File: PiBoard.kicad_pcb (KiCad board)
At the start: 4 copper layers, 95.7 x 102.3 mm, 171 parts, among them IC1 TCAN337DCNR, IC2 TPS2066TDGNRQ1, IC3 TPS2066TDGNRQ1, IC4 AP64501QSP-13, IC5 74LVC1G07QSE-7, IC6 TPS2553QDBVRQ1, IC8 LM76202QPWPRQ1, J1 CarPowerConnector, J10 M8 USB Conn, J11 CarCANConnector, J12 RTC Battery Port, J2 CarCANConnector, J3 2222, J4 USB_OTG, J5 M8 USB Conn, J6 M8 USB Conn, J7 Molex 470531000, J8 M8 USB Conn, J9 HDMI_E, SW1 SW_Push, SW2 SW_Push, SW3 SW_Push, U1 RTC PCF8563T, U10 Fan PWM Controller, U13 CDSOT23-T24CAN, U14 MCP2515-E/STVAO, U2 TLV71311PDBV, U3 FSUSB42MUX, U4 TUSB4041IPAPQ1, U5 TPD4EUSB30, U6 TPD4EUSB30, U7 TPD4EUSB30, Y1 24MHz Crystal, Y4 8 MHz, Y6 ECS-.327-6

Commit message: moved some stuff around
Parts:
- C14, C17, C18, C22, C23, C24, C25, C26, C27, C3, C32, C33, C36, C37, C43, C51, C54, C56, C59, C60, D10, D6, F1, F2, F3, F4, FB1, FB2, FB3, FB4, FB5, FB6, IC6, R11, R14, R16, R17, R18, R19, R2, R21, R22, R23, R27, R28, R30, R31, R32, R34, R40, R43, U13, Y6: moved to B.Cu
- C6, R55, R56: moved to F.Cu
- R44: value 5k -> 10k
- R46: value 6.8k -> 12k
- moved R41 82.9 mm to (234.5, 153.2)
- moved R43 79.6 mm to (232.7, 150.5), turned to 180 degrees
- moved R8 74.6 mm to (231.8, 154.4), turned to 0 degrees
- moved R40 74.6 mm to (229.3, 150.5), turned to 0 degrees
- moved D11 73.9 mm to (235.5, 147.8), turned to -90 degrees
- moved R46 73.9 mm to (235.5, 149.8), turned to 90 degrees
- moved IC8 73.5 mm to (230.6, 149.5), turned to 90 degrees
- moved C3 71.9 mm to (227.7, 106.6)
- moved C54 70.9 mm to (232.7, 148.5), turned to 180 degrees
- moved R27 70.2 mm to (227.6, 110.0)
- moved R42 67.5 mm to (229.2, 144.5), turned to 0 degrees
- moved R7 66.6 mm to (226.7, 151.8), turned to -90 degrees
- moved IC6 65.9 mm to (224.8, 107.4)
- moved C43 65.6 mm to (224.4, 104.2), turned to 0 degrees
- moved R28 65.0 mm to (224.7, 110.4), turned to 180 degrees
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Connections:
- net +12V renamed +24V
- net +12V_EXT renamed +24V_EXT
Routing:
- net /Board_En: track 91.5 -> 0.00 mm
- net /CM4 GPIO/GPIO3: track 76.3 -> 0.00 mm, vias 1 -> 0
- net Net-(Module1A-PI_nLED_Activity): track 69.3 -> 0.00 mm, vias 1 -> 0
- net /CM4 GPIO/CAN_SPI_CLK: track 60.1 -> 0.00 mm, vias 1 -> 0
- net /CM4 GPIO/nPWR_LED: track 59.4 -> 0.00 mm
- net /CM4 GPIO/CAN_SPI_MOSI: track 53.3 -> 0.00 mm, vias 3 -> 0
- net /CM4 GPIO/CAN_SPI_CS: track 52.8 -> 0.00 mm, vias 2 -> 0
- net /CM4 GPIO/CAN_SPI_MISO: track 51.5 -> 0.00 mm, vias 3 -> 0
- net /HDMI and High Speed/HDMI0_CK_N: track 50.2 -> 0.00 mm
- net /HDMI and High Speed/HDMI0_CK_P: track 50.1 -> 0.00 mm
- net Net-(IC1-CANH): track 50.0 -> 0.00 mm, vias 1 -> 0
- net /CM4 GPIO/CAN_INTR: track 49.4 -> 0.00 mm
- net /USB2.0 HS Hub/USB_Ports/USB_4P: track 48.2 -> 0.00 mm, vias 1 -> 0
- net /USB2.0 HS Hub/USB_Ports/USB_4N: track 46.7 -> 0.00 mm, vias 1 -> 0
- net /USB2.0 HS Hub/USB_Upstream_N: track 46.6 -> 0.00 mm, vias 2 -> 0
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
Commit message: layout draft
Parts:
- removed C18, C19, C29, C32, C33, C34, C35, C38, C39, C40, C41, C42, C44, C45, C46, C47, C48, C49: 100n, Capacitor_SMD:C_0805_2012Metric
- removed C26, C27: 25p, Capacitor_SMD:C_0805_2012Metric
- removed C28: 1u, Capacitor_SMD:C_0805_2012Metric
- removed C30, C31: 1n, Capacitor_SMD:C_0805_2012Metric
- removed F1, F2, F3, F4: 500mA, Fuse:Fuse_1206_3216Metric
- removed FB3, FB4, FB5, FB6: FerriteBead, Inductor_SMD:L_1206_3216Metric
- removed IC3: TPS2066TDGNRQ1, Controls_Pi:SOP65P490X110-9N
- removed J10, J6, J8: M8 USB Conn, Controls_Pi:321720912
- removed R13, R14, R33, R55, R56: 10k, Resistor_SMD:R_0805_2012Metric
- removed R15, R20: 1M, Resistor_SMD:R_0805_2012Metric
- removed R36, R50, R51, R52, R53, R54: 4.7k, Resistor_SMD:R_0805_2012Metric
- removed U2: TLV71311PDBV, Package_TO_SOT_SMD:SOT-23-5
- removed U4: TUSB4041IPAPQ1, Controls_Pi:PAP64_4P15X4P15_TEX
- removed U5, U6, U7: TPD4EUSB30, Package_SON:USON-10_2.5x1.0mm_P0.5mm
- removed Y1: 24MHz Crystal, Controls_Pi:ABM8AIG25000MHZ122ZT3
- added C57: 100n, Capacitor_SMD:C_0805_2012Metric, B.Cu at (176.2, 94.3)
- added C58: 10uF, Capacitor_SMD:C_0805_2012Metric, F.Cu at (149.3, 56.5)
- added D15: ESD204DQAR, Controls_Pi:ESD204DQAR, F.Cu at (180.7, 92.1)
- added D18: ESD204DQAR, Controls_Pi:ESD204DQAR, F.Cu at (180.7, 79.9)
- added H1: MountingHole, MountingHole:MountingHole_3mm, F.Cu at (106.0, 55.6)
- added H2: MountingHole, MountingHole:MountingHole_3mm, F.Cu at (187.4, 55.5)
- added H3: MountingHole, MountingHole:MountingHole_3mm, F.Cu at (106.0, 139.7)
- added H4: MountingHole, MountingHole:MountingHole_3mm, F.Cu at (187.6, 139.1)
- added IC7: TPS2553QDBVRQ1, Controls_Pi:SOT95P280X145-6N, F.Cu at (176.1, 97.5)
- added J13: RTC Battery Conn, Controls_Pi:CONN02_530470210_MOL, F.Cu at (185.1, 64.3)
- added R37: 5.1k, Resistor_SMD:R_0805_2012Metric, B.Cu at (188.4, 94.2)
- added R38: 5.1k, Resistor_SMD:R_0805_2012Metric, B.Cu at (188.4, 90.8)
- added R62: 100n, Resistor_SMD:R_0805_2012Metric, F.Cu at (173.1, 97.4)
- added R69: 82k, Resistor_SMD:R_0805_2012Metric, B.Cu at (177.1, 101.4)
- C1, C10, C12, C2, C20, C21, R24, R26, R29, R3, R41: moved to B.Cu
- C13: value 100n -> 1n; moved to B.Cu
- C15: value 1n -> 100n
- D3: value SD12_SOD323 -> SD24C_SOD323
- D6, U13: moved to F.Cu
- D9: value 12V PWR LED -> 24V PWR LED
- IC2: value TPS2066TDGNRQ1 -> TPS2553QDBVRQ1; footprint Controls_Pi:SOP65P490X110-9N -> Controls_Pi:SOT95P280X145-6N
- J4: value USB_OTG -> USB_C_Receptacle_USB2.0_16P; footprint Connector_USB:USB_Micro-B_Molex-105017-0001 -> Connector_USB:USB_C_Receptacle_GCT_USB4105-xx-A_16P_TopMnt_Horizontal
- J5: value M8 USB Conn -> USB_C_Receptacle_USB2.0_16P; footprint Controls_Pi:321720912 -> Connector_USB:USB_C_Receptacle_GCT_USB4105-xx-A_16P_TopMnt_Horizontal
- R10: value 1M -> 5.1k; moved to B.Cu
- R11: value 90.9k -> 1M
- R12: value 9.53k -> 1M; moved to B.Cu
- R40: value 1k -> 10k; moved to F.Cu
- R46: value 12k -> 10k
- R5: value 1M -> 100n; moved to F.Cu
- R6: value 1M -> 82k
- R7: value 100k -> 200k
- R8: value 200 -> 2k
- R9: value 2.2k -> 5.1k; moved to B.Cu
- moved C16 169.3 mm to (190.7, 76.7), turned to -90 degrees
- moved C17 162.9 mm to (190.7, 83.8)
- moved J5 158.0 mm to (187.6, 80.2), turned to 90 degrees
- moved FB2 157.8 mm to (181.5, 97.1)
- moved R6 154.3 mm to (176.7, 88.8), turned to 90 degrees
- moved FB1 154.1 mm to (181.2, 84.8)
- moved C15 151.6 mm to (186.5, 97.0), turned to 90 degrees
- moved R5 148.4 mm to (172.8, 84.8), turned to 90 degrees
- moved R9 147.0 mm to (186.6, 82.2)
- moved J7 143.8 mm to (177.2, 57.0), turned to 180 degrees
- moved C13 142.5 mm to (186.6, 88.0), turned to -90 degrees
- moved J4 141.8 mm to (187.5, 92.9), turned to 90 degrees
- moved IC2 140.7 mm to (175.7, 84.8), turned to -90 degrees
- moved C12 140.2 mm to (179.2, 96.5), turned to -90 degrees
- moved U1 138.9 mm to (178.9, 63.3), turned to 180 degrees
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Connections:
- C1 pad 1: +5V -> Net-(IC2-EN)
- C12 pad 1: +5V -> Net-(C12-Pad1)
- C13 pad 1: +5V -> GNDPWR
- C17 pad 1: Net-(C17-Pad1) -> GNDPWR
- C2 pad 1: +1V1 -> +5V
- C4 pad 1: Net-(C38-Pad1) -> Net-(C4-Pad1)
- D10 pad 1: /HDMI and High Speed/HDMI0_CK_N -> /HDMI and High Speed/HDMI0_CK_P
- D10 pad 10: /HDMI and High Speed/HDMI0_CK_PRT_N -> /HDMI and High Speed/HDMI0_CK_PRT_P
- D10 pad 2: /HDMI and High Speed/HDMI0_CK_P -> /HDMI and High Speed/HDMI0_CK_N
- D10 pad 4: /HDMI and High Speed/HDMI0_D1_N -> /HDMI and High Speed/HDMI0_D1_P
- D10 pad 5: /HDMI and High Speed/HDMI0_D1_P -> /HDMI and High Speed/HDMI0_D1_N
- D10 pad 6: /HDMI and High Speed/HDMI0_D1_PRT_P -> /HDMI and High Speed/HDMI0_D1_PRT_N
- D10 pad 7: /HDMI and High Speed/HDMI0_D1_PRT_N -> /HDMI and High Speed/HDMI0_D1_PRT_P
- D10 pad 9: /HDMI and High Speed/HDMI0_CK_PRT_P -> /HDMI and High Speed/HDMI0_CK_PRT_N
- FB1 pad 1: /USB2.0 HS Hub/USB_Ports/VBUS1 -> /USB2.0 high speed/VBUS_Hub
- FB1 pad 2: Net-(C17-Pad1) -> Net-(C4-Pad1)
- FB2 pad 1: /USB2.0 HS Hub/USB_Ports/VBUS2 -> /USB2.0 high speed/VBUS_Debug
- FB2 pad 2: Net-(C18-Pad1) -> Net-(C12-Pad1)
- IC2 pad 1: GND -> +5V
- IC2 pad 2: +5V -> GND
- IC2 pad 3: /USB2.0 HS Hub/USB_Ports/EN1 -> Net-(IC2-EN)
- IC2 pad 4: /USB2.0 HS Hub/USB_Ports/EN2 -> Net-(IC2-EN)
- IC2 pad 5: /USB2.0 HS Hub/USB_Ports/OC2 -> Net-(IC2-ILIM)
- IC2 pad 6: Net-(IC2-OUT2) -> /USB2.0 high speed/VBUS_Hub
- J11 pad 1: Net-(IC1-CANH) -> Net-(IC1-CANL)
- J11 pad 2: Net-(IC1-CANL) -> Net-(IC1-CANH)
- J2 pad 1: Net-(IC1-CANH) -> Net-(IC1-CANL)
- J2 pad 2: Net-(IC1-CANL) -> Net-(IC1-CANH)
- R10 pad 1: Net-(U4A-XI) -> Net-(C4-Pad1)
- R10 pad 2: Net-(U4A-XO) -> Net-(J5-CC2)
- R11 pad 1: +5V -> GND
- R11 pad 2: Net-(U4A-USB_VBUS) -> GNDPWR
- R12 pad 1: Net-(U4A-USB_R1) -> GND
- R12 pad 2: GND -> GNDPWR
- R5 pad 1: GND -> /Board_En
- R5 pad 2: GNDPWR -> Net-(IC2-EN)
- R6 pad 2: GNDPWR -> Net-(IC2-ILIM)
- R9 pad 1: Net-(J4-VBUS) -> Net-(C4-Pad1)
- R9 pad 2: /HDMI and High Speed/USBOTG_ID -> Net-(J5-CC1)
- U3 pad 6: /USB2.0 HS Hub/USB_Upstream_N -> /USB2.0 high speed/USB_Hub_Up_N
- U3 pad 7: /USB2.0 HS Hub/USB_Upstream_P -> /USB2.0 high speed/USB_Hub_Up_P
- U3 pad 8: Net-(J4-D-) -> /USB2.0 high speed/USB_Debug_N
- U3 pad 9: Net-(J4-D+) -> /USB2.0 high speed/USB_Debug_P
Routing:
- net /CM4 GPIO/CAN_SPI_MOSI: track 0.00 -> 65.4 mm, vias 0 -> 1
- net /CM4 GPIO/CAN_SPI_MISO: track 0.00 -> 65.2 mm, vias 0 -> 1
- net /CM4 GPIO/CAN_SPI_CLK: track 0.00 -> 60.5 mm, vias 0 -> 1
- net /CM4 GPIO/GPIO22: track 0.00 -> 58.2 mm, vias 0 -> 1
- net /CM4 GPIO/GPIO17: track 0.00 -> 54.5 mm, vias 0 -> 1
- net /CM4 GPIO/GPIO27: track 0.00 -> 53.5 mm, vias 0 -> 1
- net /CM4 GPIO/GPIO0: track 0.00 -> 53.2 mm, vias 0 -> 1
- net /CM4 GPIO/GPIO6: track 0.00 -> 49.7 mm, vias 0 -> 1
- net /CM4 GPIO/GPIO5: track 0.00 -> 48.4 mm, vias 0 -> 1
- net /CM4 GPIO/GPIO4: track 0.00 -> 47.3 mm, vias 0 -> 1
- net /CM4 GPIO/GPIO3: track 0.00 -> 46.4 mm, vias 0 -> 1
- net /CM4 GPIO/GPIO13: track 0.00 -> 44.9 mm, vias 0 -> 1
- net /CM4 GPIO/GPIO19: track 0.00 -> 40.2 mm, vias 0 -> 1
- net /CM4 GPIO/GPIO2: track 0.00 -> 37.9 mm, vias 0 -> 1
- net /CM4 GPIO/GPIO26: track 0.00 -> 35.5 mm, vias 0 -> 1
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- added copper zone on B.Cu, net GND
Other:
- board size 95.7 x 102.3 mm -> 90.1 x 92.5 mm
- board text added: "Trying to keep this space more open for fancy routing ig"

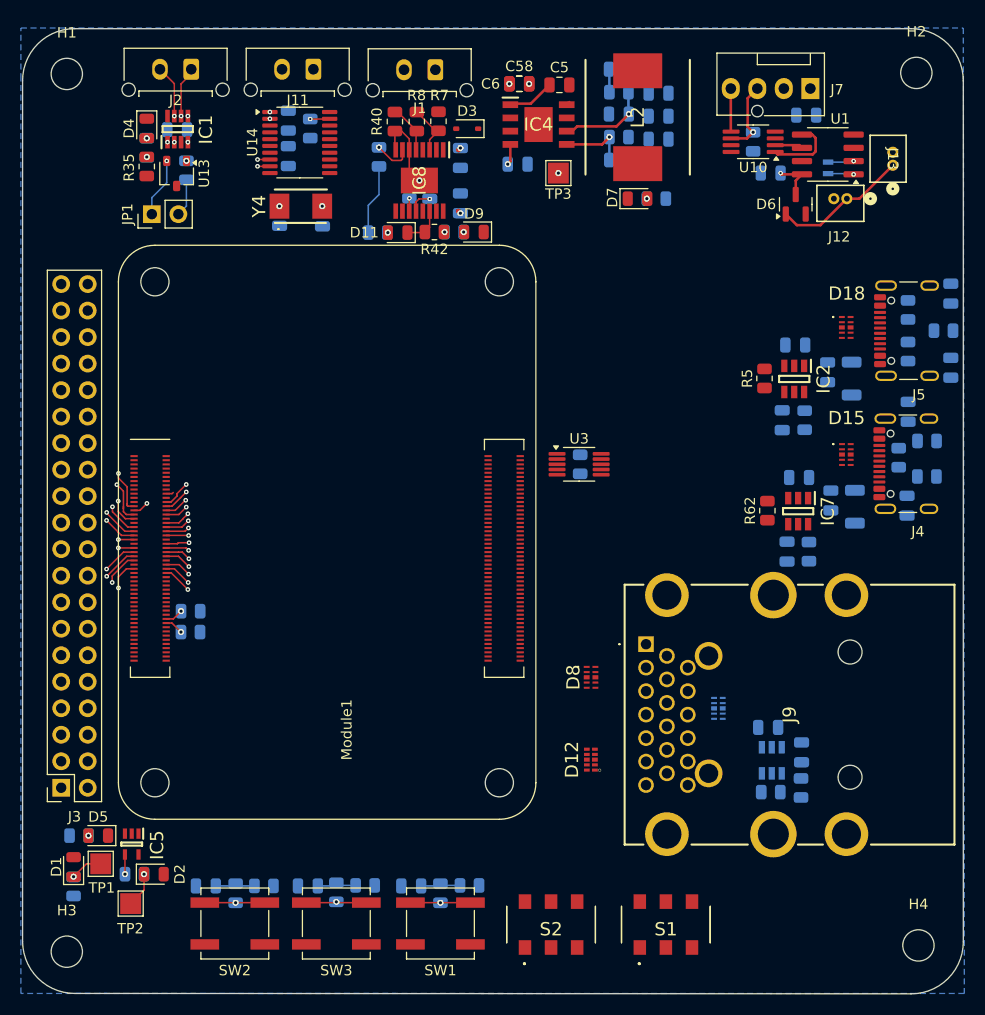
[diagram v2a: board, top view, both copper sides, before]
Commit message: moved everything to front & 0603'd stuff
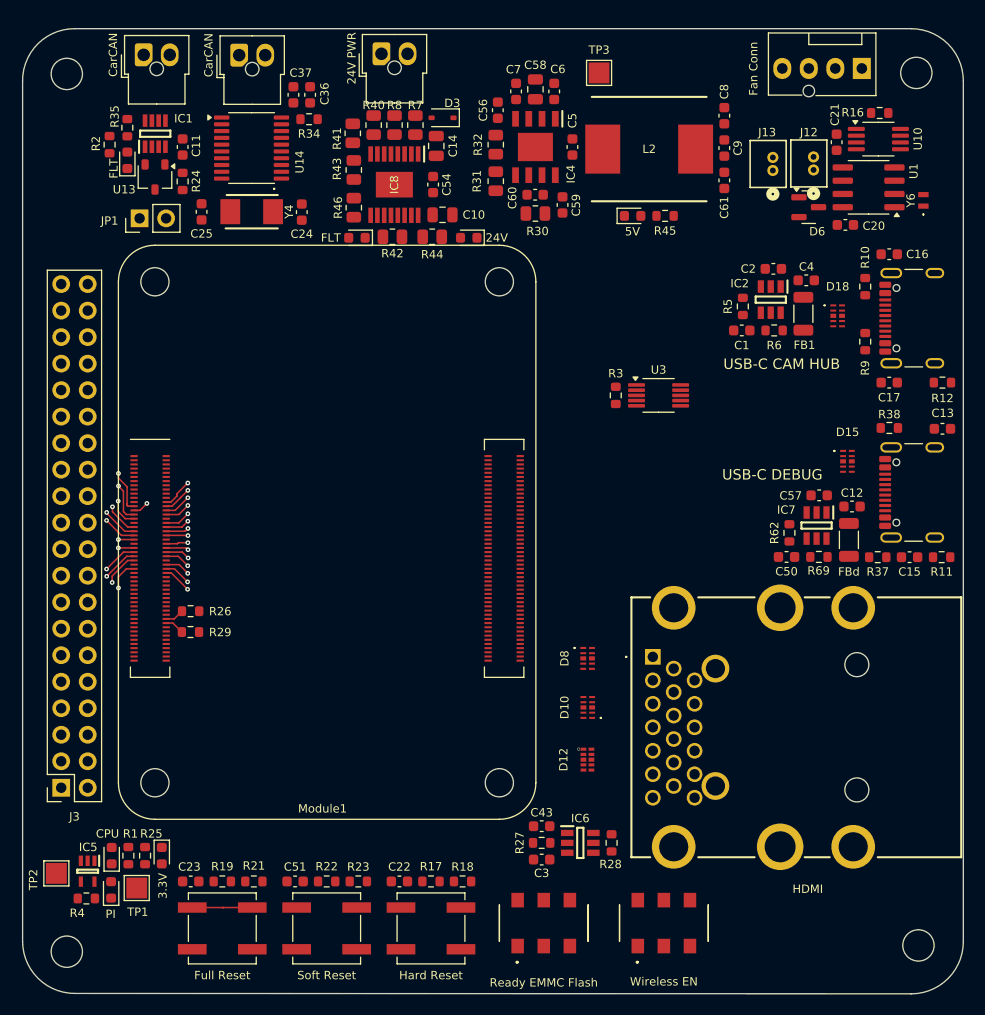
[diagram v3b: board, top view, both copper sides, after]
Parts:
- removed J11, J2: CarCANConnector, Connector_Molex:Molex_Micro-Fit_3.0_43650-0215_1x02_P3.00mm_Vertical
- added CarCAN: CarCANConnector, UTSVT_Connectors:Molex_Nano-Fit_105309-xx02_1x02_P2.50mm_Vertical, F.Cu at (113.4, 53.8)
- added CarCAN: CarCANConnector, UTSVT_Connectors:Molex_Nano-Fit_105309-xx02_1x02_P2.50mm_Vertical, F.Cu at (122.5, 53.8)
- 24V: renamed from D9; footprint LED_SMD:LED_0805_2012Metric -> LED_SMD:LED_0603_1608Metric
- 24V PWR: renamed from J1; footprint Connector_Molex:Molex_Micro-Fit_3.0_43650-0215_1x02_P3.00mm_Vertical -> UTSVT_Connectors:Molex_Nano-Fit_105309-xx02_1x02_P2.50mm_Vertical
- 3.3V: renamed from D5; footprint LED_SMD:LED_0805_2012Metric -> LED_SMD:LED_0603_1608Metric
- 5V: renamed from D7; footprint LED_SMD:LED_0805_2012Metric -> LED_SMD:LED_0603_1608Metric
- C1, C11, C12, C13, C15, C16, C17, C2, C20, C21, C22, C23, C24, C25, C3, C36, C37, C4, C43, C50, C51, C54, C56, C57, C59, C60, C61, C7, C8, C9: footprint Capacitor_SMD:C_0805_2012Metric -> Capacitor_SMD:C_0603_1608Metric; moved to F.Cu
- C10, C14, D10, FB1, IC6, R30, R31, R32, R41, R43, R44, R46, Y6: moved to F.Cu
- C5, C6: footprint Capacitor_SMD:C_0805_2012Metric -> Capacitor_SMD:C_0603_1608Metric
- CPU: renamed from D1; footprint LED_SMD:LED_0805_2012Metric -> LED_SMD:LED_0603_1608Metric
- FBd: renamed from FB2; moved to F.Cu
- FLT: renamed from D11; footprint LED_SMD:LED_0805_2012Metric -> LED_SMD:LED_0603_1608Metric
- FLT: renamed from D4; footprint LED_SMD:LED_0805_2012Metric -> LED_SMD:LED_0603_1608Metric
- Fan Conn: renamed from J7
- Full Reset: renamed from SW2
- Hard Reset: renamed from SW1
- PI: renamed from D2; footprint LED_SMD:LED_0805_2012Metric -> LED_SMD:LED_0603_1608Metric
- R1, R10, R11, R12, R16, R17, R18, R19, R2, R21, R22, R23, R24, R25, R26, R27, R28, R29, R3, R34, R37, R38, R4, R45, R6, R69, R9: footprint Resistor_SMD:R_0805_2012Metric -> Resistor_SMD:R_0603_1608Metric; moved to F.Cu
- R35, R5, R62: footprint Resistor_SMD:R_0805_2012Metric -> Resistor_SMD:R_0603_1608Metric
- Ready EMMC Flash: renamed from S2
- Soft Reset: renamed from SW3
- USB-C CAM HUB: renamed from J5
- USB-C DEBUG: renamed from J4
- Wireless EN: renamed from S1
- moved C3 26.9 mm to (151.5, 130.9), turned to 180 degrees
- moved R27 25.4 mm to (151.5, 129.3), turned to 0 degrees
- moved C43 23.7 mm to (151.5, 127.7), turned to 180 degrees
- moved IC6 20.0 mm to (155.2, 129.3), turned to 0 degrees
- moved R28 16.0 mm to (158.2, 129.3), turned to 90 degrees
- moved R30 14.1 mm to (150.9, 69.0), turned to 0 degrees
- moved C59 14.1 mm to (153.5, 68.2), turned to 90 degrees
- moved D10 12.5 mm to (155.9, 116.3), turned to 180 degrees
- moved R16 12.4 mm to (183.9, 59.3), turned to 0 degrees
- moved U10 12.0 mm to (183.8, 61.8), turned to 0 degrees
- moved R31 12.0 mm to (147.1, 65.9), turned to 90 degrees
- moved R32 11.8 mm to (147.1, 62.4), turned to 90 degrees
- moved C25 11.6 mm to (118.9, 68.8), turned to -90 degrees
- moved J13 11.5 mm to (173.7, 64.8)
- moved C60 11.1 mm to (150.9, 67.2), turned to 0 degrees
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- renumbered J9 to HDMI
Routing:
- net Net-(IC1-CANH): track 28.5 -> 0.00 mm, vias 2 -> 0
- net Net-(IC1-CANL): track 22.2 -> 0.00 mm, vias 2 -> 0
- net /RTC and Fan/RED: track 13.1 -> 0.00 mm
- net /CarCAN/CAN_TX: track 11.0 -> 0.00 mm, vias 2 -> 0
- net /Power Distribution/RTN: track 9.97 -> 0.00 mm, vias 1 -> 0
- net Net-(U14-OSC1): track 9.70 -> 0.00 mm, vias 2 -> 0
- net /CarCAN/CAN_RX: track 8.79 -> 0.00 mm, vias 2 -> 0
- net Net-(IC4-COMP): track 8.74 -> 0.00 mm, vias 1 -> 0
- net Net-(J7-Pin_3): track 7.14 -> 0.00 mm, vias 1 -> 0
- net +24V_EXT: track 7.01 -> 0.00 mm, vias 1 -> 0
- net Net-(U14-OSC2): track 6.98 -> 0.00 mm, vias 2 -> 0
- net /CM4 GPIO/SDA0: track 8.58 -> 1.86 mm, vias 1 -> 0
- net Net-(IC4-FB): track 6.58 -> 0.00 mm, vias 1 -> 0
- net /CarCAN/Fault: track 6.38 -> 0.00 mm, vias 2 -> 0
- net Net-(R22-Pad1): track 5.81 -> 0.00 mm, vias 1 -> 0
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- removed copper zone on B.Cu, net GND
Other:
- board text added: "Left some of these pwr components 0805 (?)"

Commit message: mostly routed, except highspeed
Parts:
- removed J13: RTC Battery Conn, Controls_Pi:CONN02_530470210_MOL
- moved C61 36.9 mm to (133.0, 57.8), turned to 90 degrees
- moved C8 36.3 mm to (133.0, 64.0), turned to -90 degrees
- moved C9 36.0 mm to (133.0, 60.9), turned to -90 degrees
- moved R45 28.8 mm to (138.7, 54.4), turned to 0 degrees
- moved C14 28.7 mm to (170.1, 63.4)
- moved 24V 28.5 mm to (173.0, 72.9)
- moved R44 28.4 mm to (169.3, 72.9)
- moved R42 28.3 mm to (165.4, 72.9)
- moved D3 27.5 mm to (169.5, 59.7)
- moved FLT 27.4 mm to (161.1, 73.1)
- moved C10 27.3 mm to (169.3, 70.2)
- moved C54 27.3 mm to (168.4, 67.0)
- moved R7 27.2 mm to (166.6, 60.9)
- moved 24V PWR 26.9 mm to (163.1, 53.7)
- moved R8 26.9 mm to (164.3, 60.9)
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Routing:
- net GND: track 0.00 -> 187.0 mm, vias 0 -> 67
- net /Board_En: track 0.00 -> 129.2 mm, vias 0 -> 4
- net /CM4 GPIO/SDA0: track 1.86 -> 104.3 mm, vias 0 -> 4
- net /CM4 GPIO/SCL0: track 1.82 -> 99.6 mm, vias 0 -> 4
- net +3.3V: track 0.00 -> 78.4 mm, vias 0 -> 3
- net /CM4 GPIO/EEPROM_nWP: track 0.00 -> 77.9 mm, vias 0 -> 3
- net /CM4 GPIO/BT_Disable: track 0.00 -> 73.6 mm, vias 0 -> 3
- net /CM4 GPIO/WiFi_Disable: track 0.00 -> 71.8 mm, vias 0 -> 3
- net +5V: track 0.00 -> 61.6 mm, vias 0 -> 1
- net /CM4 GPIO/nRPIBOOT: track 0.00 -> 59.2 mm, vias 0 -> 3
- net GNDPWR: track 0.00 -> 52.3 mm
- net /CM4 GPIO/CAN_SPI_CS: track 6.85 -> 55.9 mm, vias 1 -> 4
- net /CM4 GPIO/RUN_PG: track 0.00 -> 48.4 mm, vias 0 -> 4
- net /CM4 GPIO/CAN_SPI_MOSI: track 65.4 -> 111.0 mm, vias 1 -> 2
- net /CM4 GPIO/CAN_SPI_CLK: track 60.6 -> 104.1 mm, vias 1 -> 4
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- added copper zone on F.Cu, net +24V
- added copper zone on F.Cu, net +24V_EXT
- added copper zone on F.Cu, net +3.3V
- added copper zone on F.Cu, net +5V
- added copper zone on B.Cu, net GND
- added copper zone on In1.Cu, net GND

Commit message: added new power, but lowkey need to redo a bunch of shit
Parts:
- removed 24V: 24V PWR LED, LED_SMD:LED_0603_1608Metric
- removed 24V PWR: CarPowerConnector, UTSVT_Connectors:Molex_Nano-Fit_105309-xx02_1x02_P2.50mm_Vertical
- removed C10, C14: 10u, Capacitor_SMD:C_0805_2012Metric
- removed C54: 100n, Capacitor_SMD:C_0603_1608Metric
- removed D3: SD24C_SOD323, Diode_SMD:D_SOD-323
- removed FLT: PWR FAULT, LED_SMD:LED_0603_1608Metric
- removed IC8: LM76202QPWPRQ1, Controls_Pi:SOP65P640X120-17N
- removed R40, R41, R46: 10k, Resistor_SMD:R_0805_2012Metric
- removed R42: 100k, Resistor_SMD:R_0805_2012Metric
- removed R43: 6.65k, Resistor_SMD:R_0805_2012Metric
- removed R7: 200k, Resistor_SMD:R_0805_2012Metric
- removed R8: 2k, Resistor_SMD:R_0805_2012Metric
- added C18: 1u, Capacitor_SMD:C_0603_1608Metric, F.Cu at (168.3, 58.2)
- added C19: 220n, Capacitor_SMD:C_0603_1608Metric, F.Cu at (168.3, 59.8)
- added C26: 22n, Capacitor_SMD:C_0603_1608Metric, F.Cu at (156.2, 63.8)
- added C27: 220u, Capacitor_SMD:C_0603_1608Metric, F.Cu at (156.2, 66.8)
- added D9: 24V PWR LED, LED_SMD:LED_0603_1608Metric, F.Cu at (164.8, 64.8)
- added IC3: LM74502HDDFR, UTSVT_Power_SP:SOT65P280X110-8N, F.Cu at (165.1, 58.0)
- added J1: CarLVPowerConnector, UTSVT_Connectors:Molex_Nano-Fit_105309-xx02_1x02_P2.50mm_Vertical, F.Cu at (157.9, 53.7)
- added Q1: PSMN8R5-40MSDX, UTSVT_Power_SP:PSMN8R5-40MSDX, F.Cu at (159.7, 65.4)
- added R100: 10k, Resistor_SMD:R_0603_1608Metric, F.Cu at (168.3, 56.6)
- added R13: 8k, Resistor_SMD:R_0603_1608Metric, F.Cu at (165.2, 55.0)
- added R14: 200k, Resistor_SMD:R_0603_1608Metric, F.Cu at (168.3, 55.1)
- added Z1: SMAF4751A-TP, UTSVT_Passives:SODFL5026X125N, F.Cu at (166.5, 62.2)
- added Z2: SMAF4751A-TP, UTSVT_Passives:SODFL5026X125N, F.Cu at (159.3, 60.5)
- J4: renamed from USB-C DEBUG
- J5: renamed from USB-C CAM HUB
- J7: renamed from Fan Conn
- S1: renamed from Wireless EN
- S2: renamed from Ready EMMC Flash
- SW1: renamed from Hard Reset
- SW2: renamed from Full Reset
- SW3: renamed from Soft Reset
- moved R44 9.30 mm to (160.7, 69.4)
- moved C5 7.30 mm to (143.6, 67.0), turned to 180 degrees
- moved TP3 6.44 mm to (138.8, 70.0)
- moved C59 3.99 mm to (144.2, 54.3), turned to 180 degrees
- moved C56 3.22 mm to (152.2, 65.0)
- moved C58 3.22 mm to (147.9, 67.5)
- moved C6 3.22 mm to (146.1, 67.3)
- moved C60 3.22 mm to (147.9, 56.4)
- moved IC4 3.22 mm to (147.9, 61.4)
- moved R30 3.22 mm to (147.9, 54.3)
- moved R31 3.22 mm to (152.2, 58.2)
- moved R32 3.22 mm to (152.2, 61.7)
- moved C7 3.22 mm to (149.8, 67.3)
- moved C11 1.87 mm to (115.5, 62.5)
- moved C25 1.87 mm to (117.0, 68.7)
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- renumbered CPU to D1, PI to D2, FLT to D4, 3.3V to D5, 5V to D7, FBd to FB2, CarCAN to J6, CarCAN to J8, HDMI to J9
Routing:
- net +24V: track 5.45 -> 22.0 mm, vias 0 -> 1
- net Net-(IC3-GATE): track 0.00 -> 14.8 mm
- net /Power Distribution/RPP_EN: track 0.00 -> 14.0 mm
- net /Power Distribution/RTN: track 13.0 -> 0.00 mm
- net GND: track 187.0 -> 179.5 mm, vias 67 -> 70
- net Net-(IC8-~{SHDN}): track 7.28 -> 0.00 mm
- net /Power Distribution/UVLO: track 6.54 -> 0.00 mm
- net Net-(IC8-DVDT): track 6.21 -> 0.00 mm
- net /Power Distribution/OVP: track 5.68 -> 0.00 mm
- net Net-(IC8-ILIM): track 5.63 -> 0.00 mm
- net /Power Distribution/Fault: track 5.12 -> 0.00 mm
- net Net-(IC4-SW): track 5.75 -> 10.5 mm
- net Net-(IC3-OV): track 0.00 -> 4.00 mm
- net Net-(D9-A): track 1.95 -> 5.64 mm
- net Net-(D11-A): track 2.78 -> 0.00 mm
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- added copper zone on F.Cu, net /Power Distribution/LV+
- removed copper zone on F.Cu, net +24V_EXT
